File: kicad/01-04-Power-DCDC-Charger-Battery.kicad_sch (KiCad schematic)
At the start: 68 parts, among them J3 S2B-PH-K-S_LF__SN_, Q1 PMOS, Q2 AO3400A, Q3 AO3400A, U2 MCP73831-2-OT, U3 BQ29700DSER, U4 TLV62568DBVR

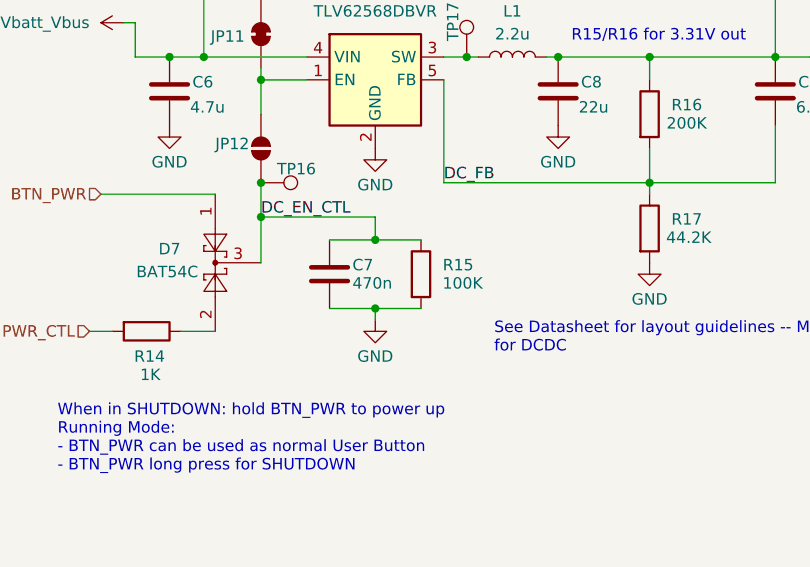
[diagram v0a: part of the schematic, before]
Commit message: DR SYS-05-MCU XTAL
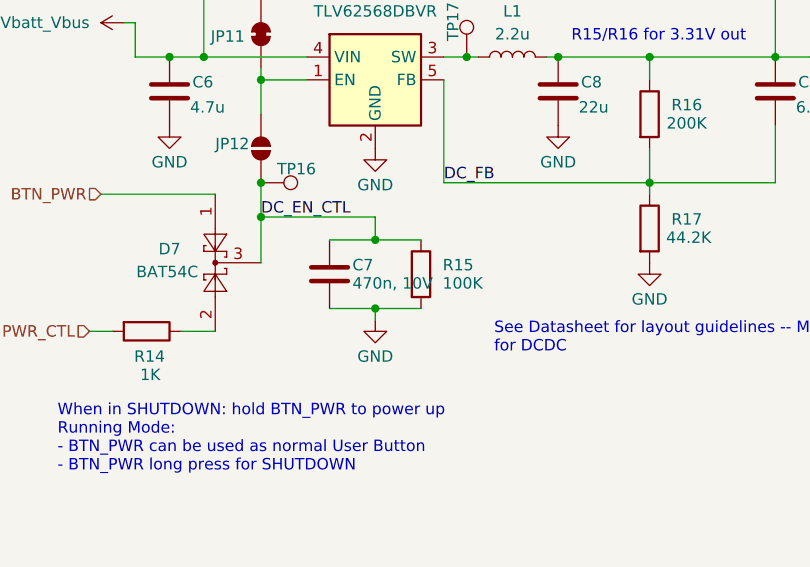
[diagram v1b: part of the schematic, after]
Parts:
- C7: value 470n -> 470n, 10V
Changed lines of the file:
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@@
 			)
 		)
-		(property "Value" "470n"
+		(property "Value" "470n, 10V"
 			(at 165.1 136.906 0)
 			(effects

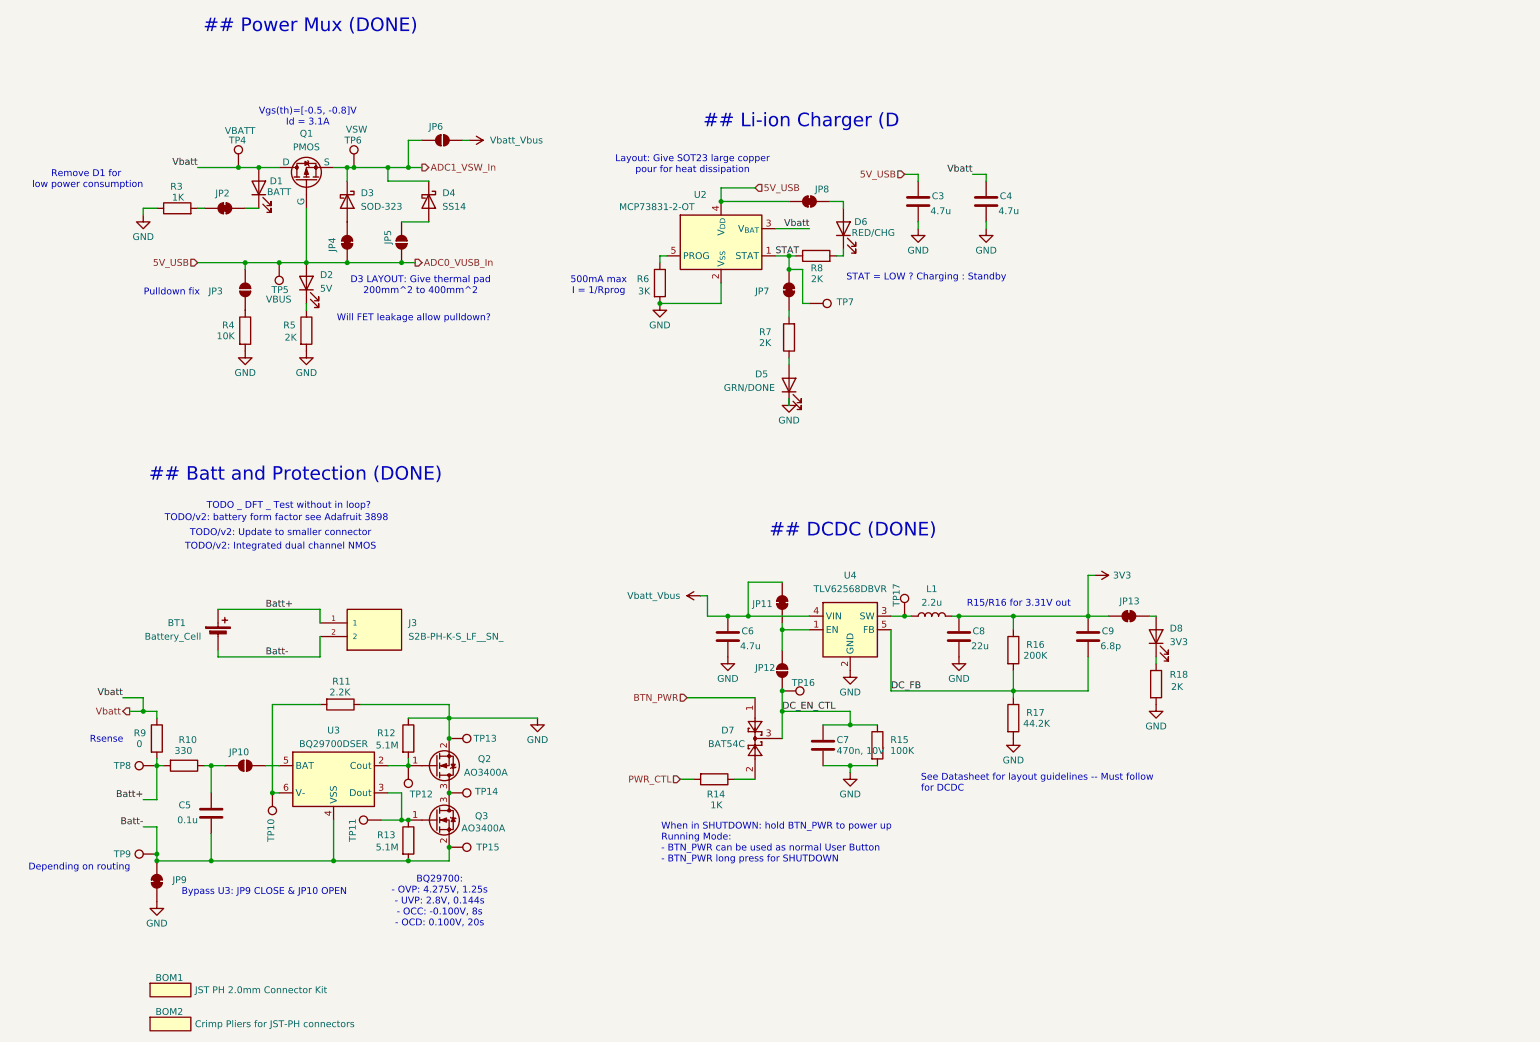
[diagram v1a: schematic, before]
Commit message: rtc new sheet, pullups
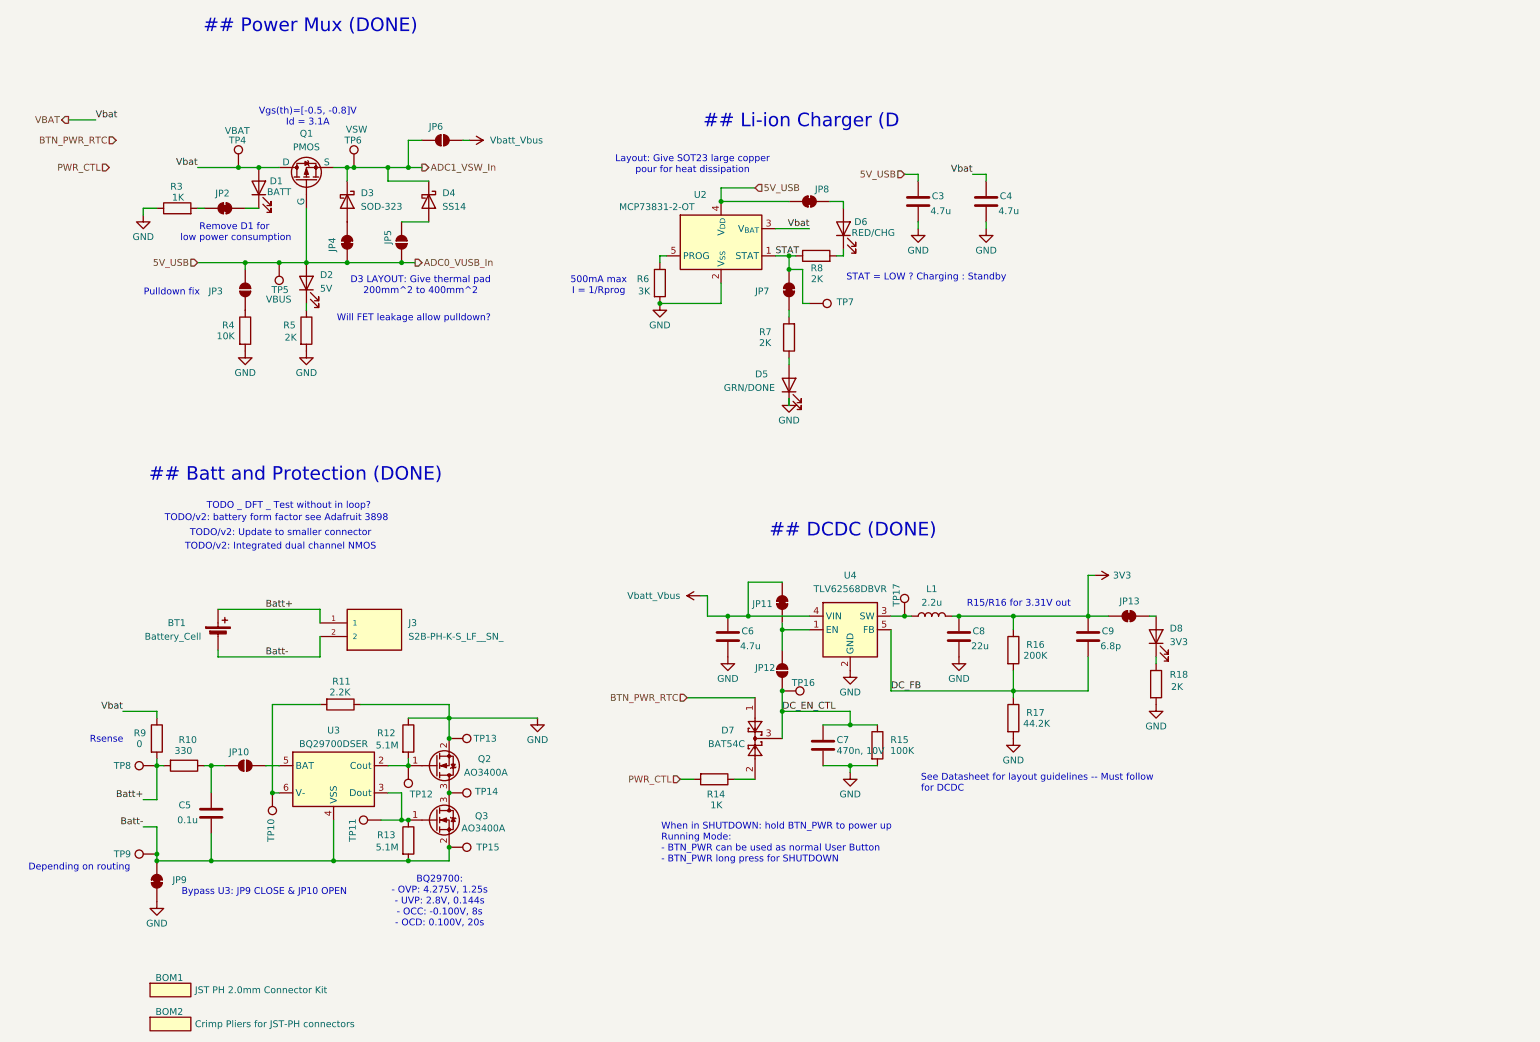
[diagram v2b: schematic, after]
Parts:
- TP4: value VBATT -> VBAT
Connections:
- net BTN_PWR renamed BTN_PWR_RTC
- net Vbatt renamed VBAT
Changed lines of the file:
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@@
 	(text "Remove D1 for\n low power consumption"
 		(exclude_from_sim no)
-		(at 24.892 30.226 0)
+		(at 52.578 40.132 0)
 		(effects
 			(font
@@
 	)
 	(junction
-		(at 35.56 129.54)
-		(diameter 0)
-		(color 0 0 0 0)
-	)
-	(junction
 		(at 92.71 130.81)
 		(diameter 0)
@@
 	(wire
 		(pts
-			(xy 31.75 127) (xy 35.56 127)
+			(xy 21.59 19.05) (xy 26.67 19.05)
+		)
+		(stroke
+			(width 0)
+			(type default)
+		)
+	)
+	(wire
+		(pts
+			(xy 31.75 129.54) (xy 38.1 129.54)
 		)
 		(stroke
@@
 	(wire
 		(pts
-			(xy 33.02 129.54) (xy 35.56 129.54)
-		)
-		(stroke
-			(width 0)
-			(type default)
-		)
-	)
-	(wire
-		(pts
 			(xy 156.21 64.77) (xy 156.21 63.5)
 		)
@@
 	(wire
 		(pts
-			(xy 35.56 129.54) (xy 38.1 129.54)
-		)
-		(stroke
-			(width 0)
-			(type default)
-		)
-	)
-	(wire
-		(pts
 			(xy 46.99 139.7) (xy 48.26 139.7)
 		)
@@
 	(wire
 		(pts
-			(xy 35.56 127) (xy 35.56 129.54)
-		)
-		(stroke
-			(width 0)
-			(type default)
-		)
-	)
-	(wire
-		(pts
 			(xy 143.51 53.34) (xy 132.08 53.34)
 		)
@@
 		)
 	)
-	(label "Vbatt"
-		(at 31.75 127 180)
+	(label "Vbat"
+		(at 31.75 129.54 180)
 		(effects
 			(font
@@
 		)
 	)
-	(label "Vbatt"
+	(label "Vbat"
 		(at 190.5 29.21 180)
 		(effects
@@
 		)
 	)
-	(label "Vbatt"
+	(label "Vbat"
+		(at 26.67 19.05 0)
+		(effects
+			(font
+				(size 1.27 1.27)
+			)
+			(justify left bottom)
+		)
+	)
+	(label "Vbat"
 		(at 160.02 39.37 180)
 		(effects
@@
 		)
 	)
-	(label "Vbatt"
+	(label "Vbat"
 		(at 45.72 27.94 180)
 		(effects
@@
 		)
 	)
+	(hierarchical_label "PWR_CTL"
+		(shape input)
+		(at 29.21 27.94 180)
+		(effects
+			(font
+				(size 1.27 1.27)
+			)
+			(justify right)
+		)
+	)
 	(hierarchical_label "ADC0_VUSB_In"
 		(shape output)
@@
 		)
 	)
-	(hierarchical_label "BTN_PWR"
+	(hierarchical_label "BTN_PWR_RTC"
 		(shape input)
 		(at 137.16 127 180)
@@
 		)
 	)
-	(hierarchical_label "Vbatt"
+	(hierarchical_label "ADC1_VSW_In"
 		(shape output)
-		(at 33.02 129.54 180)
+		(at 87.63 27.94 0)
 		(effects
 			(font
 				(size 1.27 1.27)
 			)
-			(justify right)
+			(justify left)
 		)
 	)
-	(hierarchical_label "ADC1_VSW_In"
-		(shape output)
-		(at 87.63 27.94 0)
+	(hierarchical_label "PWR_CTL"
+		(shape input)
+		(at 135.89 142.24 180)
 		(effects
 			(font
 				(size 1.27 1.27)
 			)
-			(justify left)
+			(justify right)
 		)
 	)
-	(hierarchical_label "PWR_CTL"
+	(hierarchical_label "BTN_PWR_RTC"
 		(shape input)
-		(at 135.89 142.24 180)
+		(at 30.48 22.86 180)
+		(effects
+			(font
+				(size 1.27 1.27)
+			)
+			(justify right)
+		)
+	)
+	(hierarchical_label "VBAT"
+		(shape output)
+		(at 21.59 19.05 180)
 		(effects
 			(font
@@
 			)
 		)
-		(property "Value" "VBATT"
+		(property "Value" "VBAT"
 			(at 50.8 21.082 0)
 			(effects

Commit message: pre ERC
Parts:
- removed BOM1: JST PH 2.0mm Connector Kit, symbol Project_Library:BOM_PLACEHOLDER
- removed BOM2: Crimp Pliers for JST-PH connectors, symbol Project_Library:BOM_PLACEHOLDER
- added J10: S2B-PH-K-S_LF__SN_, Connector_JST:JST_PH_S2B-PH-K_1x02_P2.00mm_Horizontal, symbol Project_Library:S2B-PH-K-S_LF__SN_
- added J11: Conn_01x02_Pin, Connector_PinHeader_2.54mm:PinHeader_1x02_P2.54mm_Vertical, symbol Connector:Conn_01x02_Pin
- added SW6: SW_SPDT, Button_Switch_THT:SW_E-Switch_EG1271_SPDT, symbol Switch:SW_SPDT
- added TP26: LOAD, project footprints:TestPoint_THTPad_D2.0mm_Drill1.0mm, symbol Connector:TestPoint
- BT1: footprint (none) -> project footprints:Battery-Holder-BH-123A_37.5P_1.8D_MH; Lab_In_Stock (none) -> Yes; MPN (Generic) -> BH-123A-A1CJ002; Manufacturer (Generic) -> MYOUNG; Supplier 1 (Generic) -> LCSC
- D1, D2, D3, D4, D8, JP13, JP2, JP3, JP4, JP5, Q1, TP4, TP5, TP6: Subsystem 01-Power-Mux -> 01A-Power-Mux
- R10, R11, R12, R13, R14, R15, R16, R17, R9: Package (none) -> 0805
- R18, R4, R5: Manufacturer (none) -> (Generic); Package (none) -> 0805; Subsystem 01-Power-Mux -> 01A-Power-Mux; Supplier 1 (none) -> (Generic)
- R3: Manufacturer (none) -> (Generic); Package (none) -> 0805; Subsystem (none) -> 04-Batt-Prot; Supplier 1 (none) -> (Generic)
- renumbered J3 to J4
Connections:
- net Batt+: now also SW6.1 (A); no longer BT1.1 (+), J4.1
- net GND: now also J10.2, J11.2 (Pin_2)
- net at D8.2 (A), JP13.1 (A): now also J10.1, J11.1 (Pin_1), TP26.1
- new net: BT1.1 (+), J4.1, SW6.2 (B)
- no-connect marks 0 -> 1
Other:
- note added: "## Batt and Protection"
- note added: "## DCDC"
- note added: "## Li-ion Charger"
- note added: "Load Test"
- note removed: "## Batt and Protection (DONE)"
- note removed: "## DCDC (DONE)"
- note removed: "## Li-ion Charger (D"
- moved on the sheet: BT1, C5, C6, C7, C8, C9, D7, D8, J4, JP10, JP11, JP12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

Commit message: ERC done
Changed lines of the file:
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@@
-	(wire
-		(pts
-			(xy 21.59 19.05) (xy 26.67 19.05)
-		)
-		(stroke
-			(width 0)
-			(type default)
-		)
-	)
 	(wire
 		(pts
@@
 	(wire
 		(pts
-			(xy 160.02 39.37) (xy 153.67 39.37)
+			(xy 156.21 39.37) (xy 153.67 39.37)
 		)
 		(stroke
@@
 		)
 	)
-	(label "Vbat"
-		(at 35.56 124.46 180)
-		(effects
-			(font
-				(size 1.27 1.27)
-			)
-			(justify right bottom)
-		)
-	)
 	(label "Batt+"
 		(at 34.29 101.6 180)
@@
 		)
 	)
-	(label "Vbat"
-		(at 190.5 29.21 180)
-		(effects
-			(font
-				(size 1.27 1.27)
-			)
-			(justify right bottom)
-		)
-	)
 	(label "Batt-"
 		(at 35.56 146.05 180)
@@
 		)
 	)
-	(label "Vbat"
-		(at 26.67 19.05 0)
-		(effects
-			(font
-				(size 1.27 1.27)
-			)
-			(justify left bottom)
-		)
-	)
-	(label "Vbat"
-		(at 160.02 39.37 180)
-		(effects
-			(font
-				(size 1.27 1.27)
-			)
-			(justify right bottom)
-		)
-	)
 	(label "STAT"
 		(at 153.67 44.45 0)
@@
 			)
 			(justify left bottom)
-		)
-	)
-	(label "Vbat"
-		(at 45.72 27.94 180)
-		(effects
-			(font
-				(size 1.27 1.27)
-			)
-			(justify right bottom)
 		)
 	)
@@
 		)
 	)
-	(hierarchical_label "PWR_CTL"
-		(shape input)
-		(at 29.21 27.94 180)
-		(effects
-			(font
-				(size 1.27 1.27)
-			)
-			(justify right)
-		)
-	)
 	(hierarchical_label "ADC0_VUSB_In"
 		(shape output)
@@
 		)
 	)
+	(hierarchical_label "VBAT"
+		(shape output)
+		(at 190.5 29.21 180)
+		(effects
+			(font
+				(size 1.27 1.27)
+			)
+			(justify right)
+		)
+	)
 	(hierarchical_label "BTN_PWR_RTC"
 		(shape input)
@@
 		)
 	)
+	(hierarchical_label "VBAT"
+		(shape output)
+		(at 156.21 39.37 0)
+		(effects
+			(font
+				(size 1.27 1.27)
+			)
+			(justify left)
+		)
+	)
 	(hierarchical_label "ADC1_VSW_In"
 		(shape output)
@@
 		)
 	)
-	(hierarchical_label "BTN_PWR_RTC"
-		(shape input)
-		(at 30.48 22.86 180)
-		(effects
-			(font
-				(size 1.27 1.27)
-			)
-			(justify right)
-		)
-	)
 	(hierarchical_label "VBAT"
 		(shape output)
-		(at 21.59 19.05 180)
+		(at 45.72 27.94 180)
 		(effects
 			(font
@@
 		)
 	)
+	(hierarchical_label "VBAT"
+		(shape output)
+		(at 35.56 124.46 180)
+		(effects
+			(font
+				(size 1.27 1.27)
+			)
+			(justify right)
+		)
+	)

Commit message: buzzer fp, power mux layout
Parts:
- removed TP5: VBUS, project footprints:TestPoint_THTPad_D2.0mm_Drill1.0mm, symbol Connector:TestPoint
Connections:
- net VBAT: now also JP2.1 (A); no longer D1.2 (A)
- net at D1.1 (K): now also R3.2; no longer JP2.1 (A)
- net at JP2.2 (B): now also D1.2 (A); no longer R3.2
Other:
- moved on the sheet: D1, JP2
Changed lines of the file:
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@@
 	)
 	(junction
+		(at 57.15 27.94)
+		(diameter 0)
+		(color 0 0 0 0)
+	)
+	(junction
 		(at 158.75 109.22)
 		(diameter 0)
@@
 	)
 	(junction
-		(at 57.15 27.94)
-		(diameter 0)
-		(color 0 0 0 0)
-	)
-	(junction
 		(at 96.52 125.73)
 		(diameter 0)
@@
 	)
 	(junction
-		(at 60.96 45.72)
-		(diameter 0)
-		(color 0 0 0 0)
-	)
-	(junction
 		(at 201.93 120.65)
 		(diameter 0)
@@
 	(wire
 		(pts
-			(xy 54.61 45.72) (xy 60.96 45.72)
-		)
-		(stroke
-			(width 0)
-			(type default)
-		)
-	)
-	(wire
-		(pts
 			(xy 66.04 104.14) (xy 72.39 104.14)
 		)
@@
 	(wire
 		(pts
-			(xy 57.15 27.94) (xy 60.96 27.94)
-		)
-		(stroke
-			(width 0)
-			(type default)
-		)
-	)
-	(wire
-		(pts
 			(xy 71.12 27.94) (xy 73.66 27.94)
 		)
@@
 	(wire
 		(pts
+			(xy 57.15 27.94) (xy 60.96 27.94)
+		)
+		(stroke
+			(width 0)
+			(type default)
+		)
+	)
+	(wire
+		(pts
 			(xy 158.75 100.33) (xy 152.4 100.33)
 		)
@@
 	(wire
 		(pts
-			(xy 60.96 45.72) (xy 66.04 45.72)
+			(xy 54.61 45.72) (xy 66.04 45.72)
 		)
 		(stroke
@@
 	(symbol
 		(lib_id "Jumper:SolderJumper_2_Bridged")
-		(at 50.8 35.56 180)
+		(at 57.15 31.75 270)
 		(unit 1)
 		(exclude_from_sim no)
@@
 		(dnp no)
 		(property "Reference" "JP2"
-			(at 49.022 32.766 0)
+			(at 54.356 33.528 0)
 			(effects
 				(font
@@
 		)
 		(property "Value" "SolderJumper_2_Bridged"
-			(at 52.0699 33.02 90)
+			(at 54.61 30.4801 90)
 			(effects
 				(font
@@
 		)
 		(property "Footprint" "Jumper:SolderJumper-2_P1.3mm_Bridged_RoundedPad1.0x1.5mm"
-			(at 50.8 35.56 0)
+			(at 57.15 31.75 0)
 			(effects
 				(font
@@
 		)
 		(property "Datasheet" "~"
-			(at 50.8 35.56 0)
+			(at 57.15 31.75 0)
 			(effects
 				(font
@@
 		)
 		(property "Description" "Solder Jumper, 2-pole, closed/bridged"
-			(at 50.8 35.56 0)
+			(at 57.15 31.75 0)
 			(effects
 				(font
@@
 		)
 		(property "Subsystem" "01A-Power-Mux"
-			(at 50.8 35.56 0)
+			(at 57.15 31.75 0)
 			(effects
 				(font
@@
 		)
 		(property "MPN" "(Embedded)"
-			(at 50.8 35.56 0)
+			(at 57.15 31.75 0)
 			(effects
 				(font
@@
 	(symbol
 		(lib_id "Device:LED")
-		(at 57.15 31.75 90)
+		(at 50.8 35.56 0)
 		(unit 1)
 		(exclude_from_sim no)
@@
 		(dnp no)
 		(property "Reference" "D1"
-			(at 59.182 30.48 90)
+			(at 49.276 31.242 0)
 			(effects
 				(font
 					(size 1.27 1.27)
 				)
-				(justify right)
+				(justify left)
 			)
 		)
 		(property "Value" "BATT"
-			(at 58.674 32.512 90)
+			(at 48.768 33.274 0)
 			(effects
 				(font
 					(size 1.27 1.27)
 				)
-				(justify right)
+				(justify left)
 			)
 		)
 		(property "Footprint" "LED_SMD:LED_0805_2012Metric"
-			(at 57.15 31.75 0)
+			(at 50.8 35.56 0)
 			(effects
 				(font
@@
 		)
 		(property "Datasheet" "~"
-			(at 57.15 31.75 0)
+			(at 50.8 35.56 0)
 			(effects
 				(font
@@
 		)
 		(property "Description" "Light emitting diode"
-			(at 57.15 31.75 0)
+			(at 50.8 35.56 0)
 			(effects
 				(font
@@
 		)
 		(property "Sim.Pins" "1=K 2=A"
-			(at 57.15 31.75 0)
+			(at 50.8 35.56 0)
 			(effects
 				(font
@@
 		)
 		(property "MPN" "KT-0805G"
-			(at 57.15 31.75 90)
+			(at 50.8 35.56 90)
 			(effects
 				(font
@@
 		)
 		(property "Manufacturer" "Hubei KENTO Elec"
-			(at 57.15 31.75 90)
+			(at 50.8 35.56 90)
 			(effects
 				(font
@@
 		)
 		(property "Supplier 1" "LCSC"
-			(at 57.15 31.75 90)
+			(at 50.8 35.56 90)
 			(effects
 				(font
@@
 		)
 		(property "Supplier 1 SKU" "C2297"
-			(at 57.15 31.75 90)
+			(at 50.8 35.56 90)
 			(effects
 				(font
@@
 		)
 		(property "Supplier 1 URL" "https://lcsc.com/product-detail/LED-Indication-Discrete_Hubei-KENTO-Elec-KT-0805G_C2297.html?s_z=n_KT-0805G"
-			(at 57.15 31.75 90)
+			(at 50.8 35.56 90)
 			(effects
 				(font
@@
 		)
 		(property "Package" "0805"
-			(at 57.15 31.75 90)
+			(at 50.8 35.56 90)
 			(effects
 				(font
@@
 		)
 		(property "Subsystem" "01A-Power-Mux"
-			(at 57.15 31.75 90)
+			(at 50.8 35.56 90)
 			(effects
 				(font
@@
 					(unit 1)
 				)
-			)
-		)
-	)
-	(symbol
-		(lib_id "Connector:TestPoint")
-		(at 60.96 45.72 180)
-		(unit 1)
-		(exclude_from_sim no)
-		(in_bom yes)
-		(on_board yes)
-		(dnp no)
-		(property "Reference" "TP5"
-			(at 62.738 50.8 0)
-			(effects
-				(font
-					(size 1.27 1.27)
-				)
-				(justify left)
-			)
-		)
-		(property "Value" "VBUS"
-			(at 63.246 52.578 0)
-			(effects
-				(font
-					(size 1.27 1.27)
-				)
-				(justify left)
-			)
-		)
-		(property "Footprint" "project footprints:TestPoint_THTPad_D2.0mm_Drill1.0mm"
-			(at 55.88 45.72 0)
-			(effects
-				(font
-					(size 1.27 1.27)
-				)
-				(hide yes)
-			)
-		)
-		(property "Datasheet" "~"
-			(at 55.88 45.72 0)
-			(effects
-				(font
-					(size 1.27 1.27)
-				)
-				(hide yes)
-			)
-		)
-		(property "Description" "test point"
-			(at 60.96 45.72 0)
-			(effects
-				(font
-					(size 1.27 1.27)
-				)
-				(hide yes)
-			)
-		)
-		(property "Subsystem" "01A-Power-Mux"
-			(at 60.96 45.72 0)
-			(effects
-				(font
-					(size 1.27 1.27)
-				)
-				(hide yes)
-			)
-		)
-		(property "MPN" "(Embedded)"
-			(at 60.96 45.72 0)
-			(effects
-				(font
-					(size 1.27 1.27)
-				)
-				(hide yes)
-			)
-		)
-		(pin "1"
-		)
-		(instances
-			(project "10k-Hour-Timer-RP2040"
-				(path "/9d26b66f-2a94-42e5-8460-016e0bf95186/9c84c2c8-9981-4486-adaf-4a40ca17b6d0"
-					(reference "TP5")
-					(unit 1)
-				)
